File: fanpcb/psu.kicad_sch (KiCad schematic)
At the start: 4 parts, among them T12V1 TestPoint

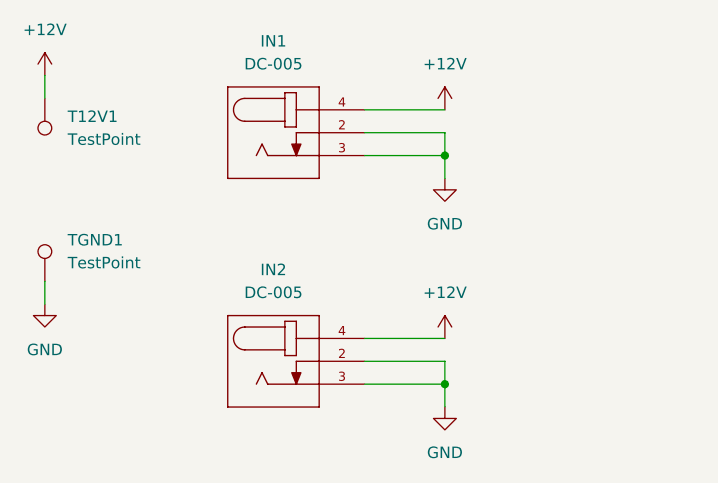
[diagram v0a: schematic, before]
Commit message: fanpcb freewheelingdiods and smoothingcapacitors
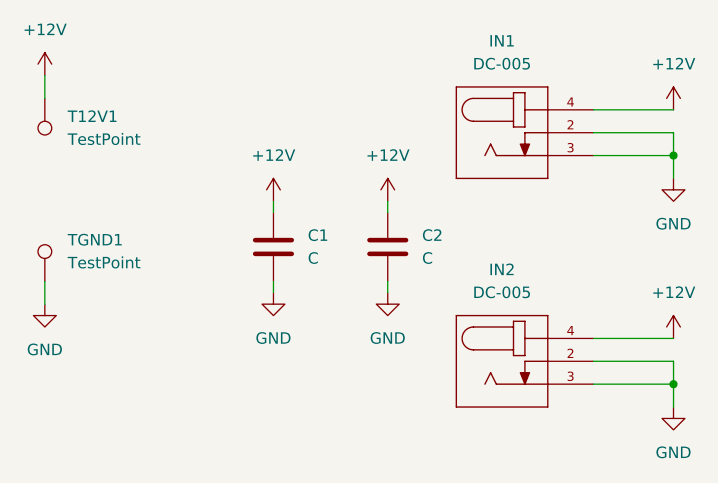
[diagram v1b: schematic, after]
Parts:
- added C1: C, Capacitor_SMD:C_1206_3216Metric_Pad1.33x1.80mm_HandSolder, symbol Device:C
- added C2: C, Capacitor_SMD:C_0603_1608Metric_Pad1.08x0.95mm_HandSolder, symbol Device:C
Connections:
- net +12V: now also C1.1, C2.1
- net GND: now also C1.2, C2.2
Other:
- moved on the sheet: IN1, IN2
